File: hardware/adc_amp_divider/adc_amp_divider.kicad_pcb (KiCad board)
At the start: 2 copper layers, 76.2 x 52.7 mm, 121 parts, among them M200 CONN_1, M201 CONN_1, M202 CONN_1, P201 CONN_10X2, P202 CONN_3, P203 CONN_2, P204 CONN_1, P205 CONN_1, P206 CONN_3, P207 CONN_2, P208 CONN_6, P209 CONN_6, U201 LMV324IDR, U202 LMV324IDR, U203 LMV324IDR

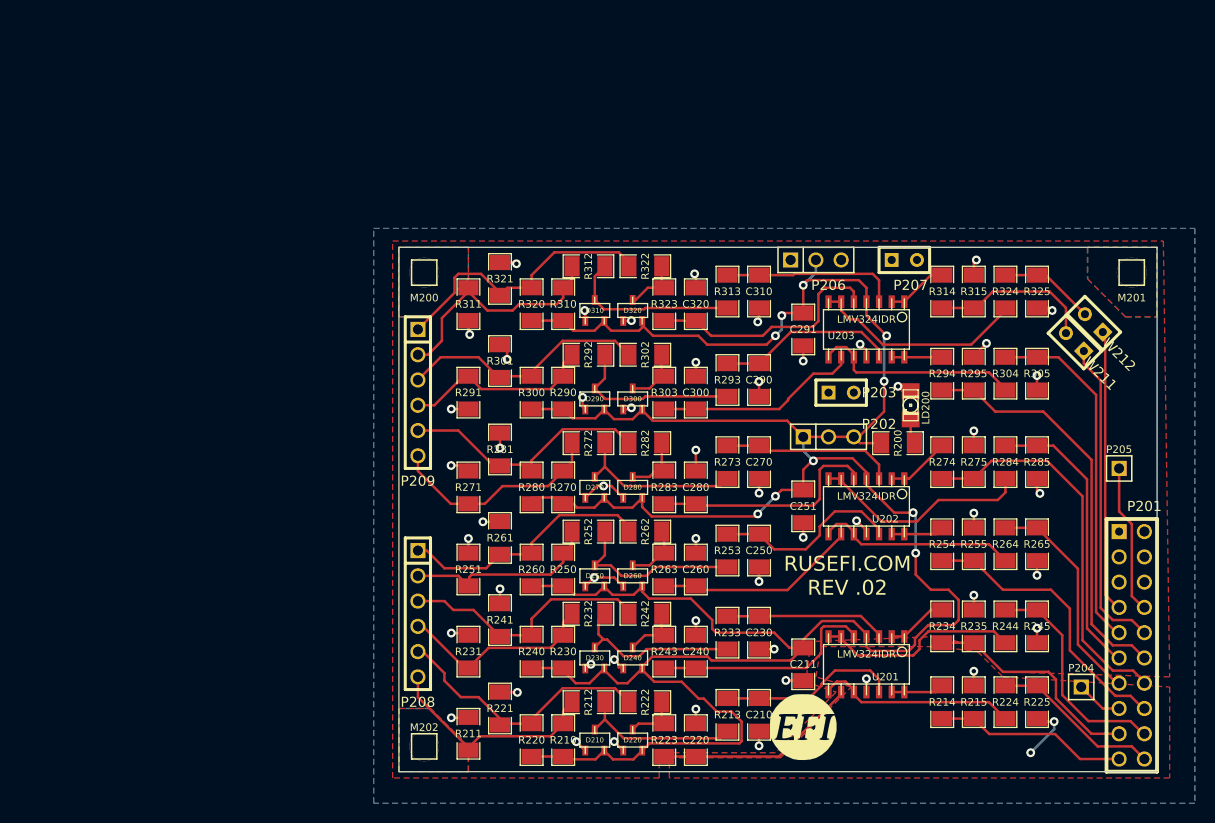
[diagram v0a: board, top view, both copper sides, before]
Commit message: 
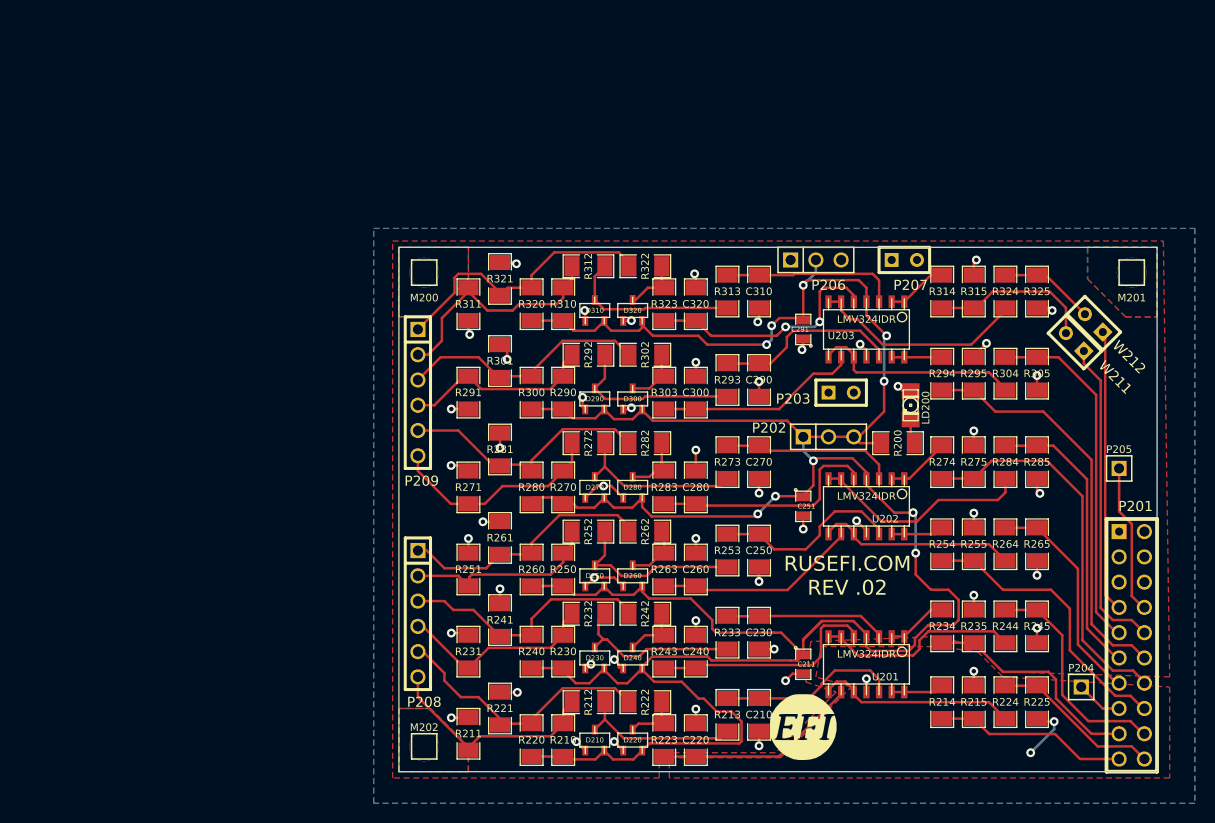
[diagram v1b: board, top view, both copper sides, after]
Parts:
- C211, C251, C291: footprint SM1206 -> SM0805
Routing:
- net VCC: track 287.5 -> 291.5 mm
- net N-000006: track 18.1 -> 18.8 mm
- net N-0000024: vias 0 -> 2

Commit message: proper location
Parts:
- moved P206 41.3 mm to (96.5, 99.7)
- moved R295 41.3 mm to (112.4, 111.1)
- moved C240 41.3 mm to (84.5, 139.1)
- moved C300 41.3 mm to (84.5, 113.0)
- moved D230 41.3 mm to (74.3, 139.7)
- moved D240 41.3 mm to (78.1, 139.7)
- moved D250 41.3 mm to (74.3, 131.4)
- moved D260 41.3 mm to (78.1, 131.4)
- moved P203 41.3 mm to (99.1, 113.0)
- moved P207 41.3 mm to (105.4, 99.7)
- moved P208 41.3 mm to (56.5, 135.3)
- moved P209 41.3 mm to (56.5, 113.0)
- moved R211 41.3 mm to (61.6, 147.3)
- moved R213 41.3 mm to (87.6, 145.4)
- moved R221 41.3 mm to (64.8, 144.8)
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
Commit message: minor improvement
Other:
- board text added: "PA1"
- board text added: "PA7"
- board text added: "PC1"
- board text added: "PC3"
- board text added: "PC5"
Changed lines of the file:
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@@
     (links 234)
     (no_connects 0)
-    (area 33.275001 96.0374 134.620001 159.545)
+    (area 33.275001 93.334999 186.700001 190.510001)
     (thickness 1.6)
-    (drawings 10)
+    (drawings 27)
     (tracks 809)
     (zones 0)
@@
     )
   )
+  (gr_text PC5 (at 123.317 150.114) (layer F.SilkS)
+    (effects (font (size 1.2 1.2) (thickness 0.3)))
+  )
+  (gr_text PA7 (at 123.3805 147.701) (layer F.SilkS)
+    (effects (font (size 1.2 1.2) (thickness 0.3)))
+  )
+  (gr_text PA1 (at 123.317 139.446) (layer F.SilkS)
+    (effects (font (size 1.2 1.2) (thickness 0.3)))
+  )
+  (gr_text PC3 (at 123.3805 137.3505) (layer F.SilkS)
+    (effects (font (size 1.2 1.2) (thickness 0.3)))
+  )
+  (gr_text PC1 (at 123.3805 134.6835) (layer F.SilkS)
+    (effects (font (size 1.2 1.2) (thickness 0.3)))
+  )
   (gr_line (start 120.65 93.345) (end 186.69 93.345) (angle 90) (layer Eco2.User) (width 0.02))
